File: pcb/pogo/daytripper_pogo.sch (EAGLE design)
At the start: 4 parts

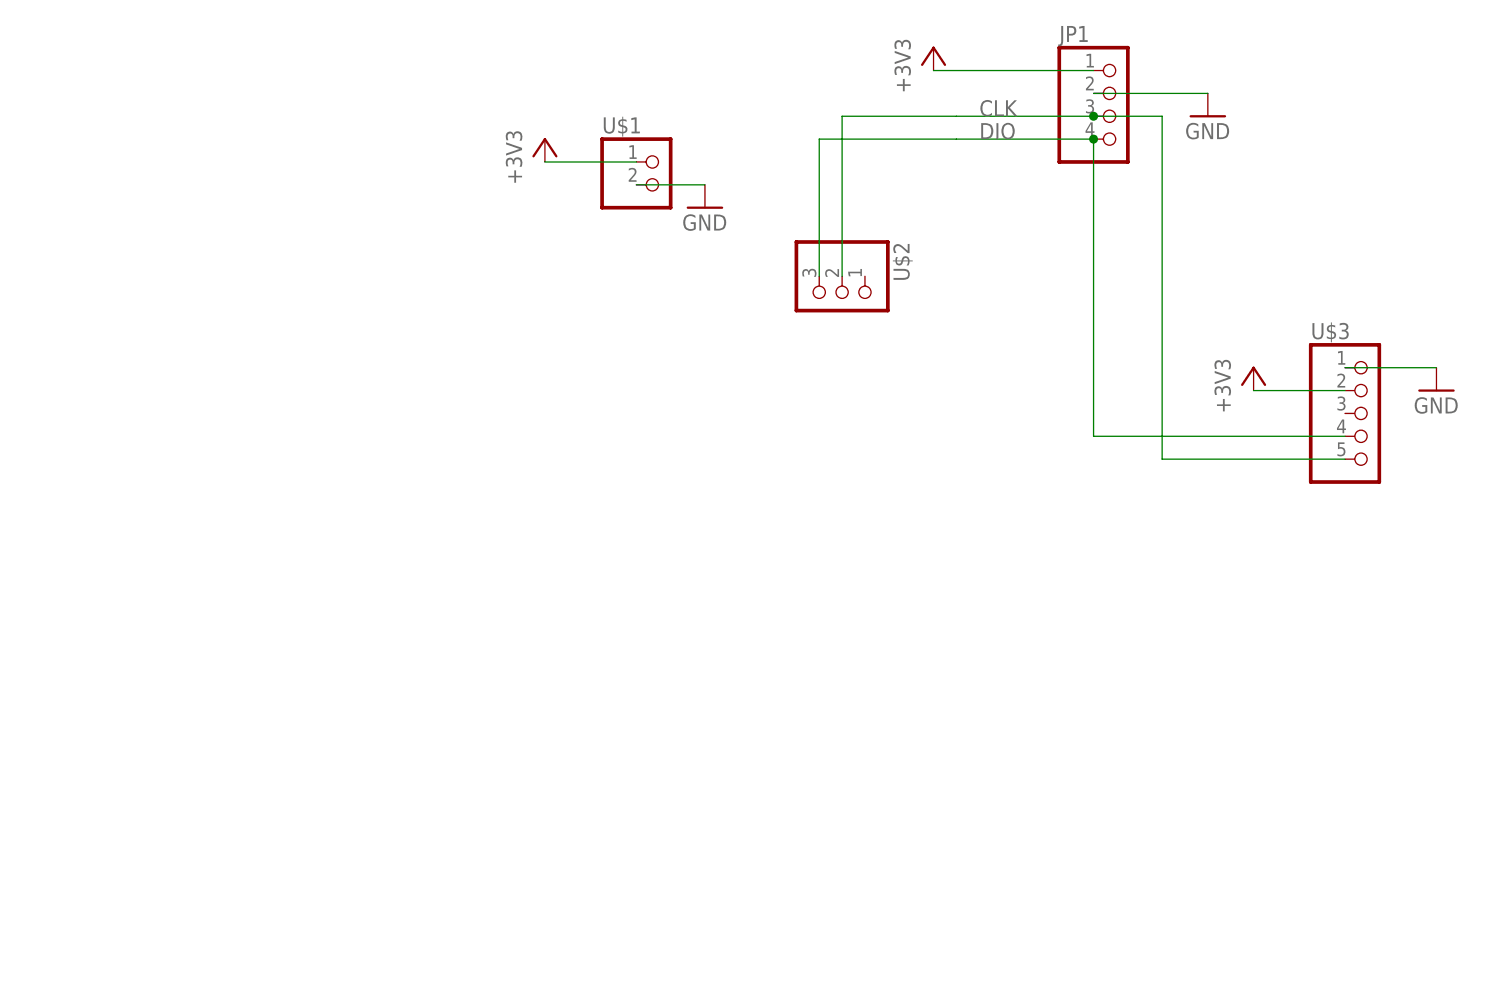
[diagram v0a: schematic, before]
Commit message: redesigned pogo board
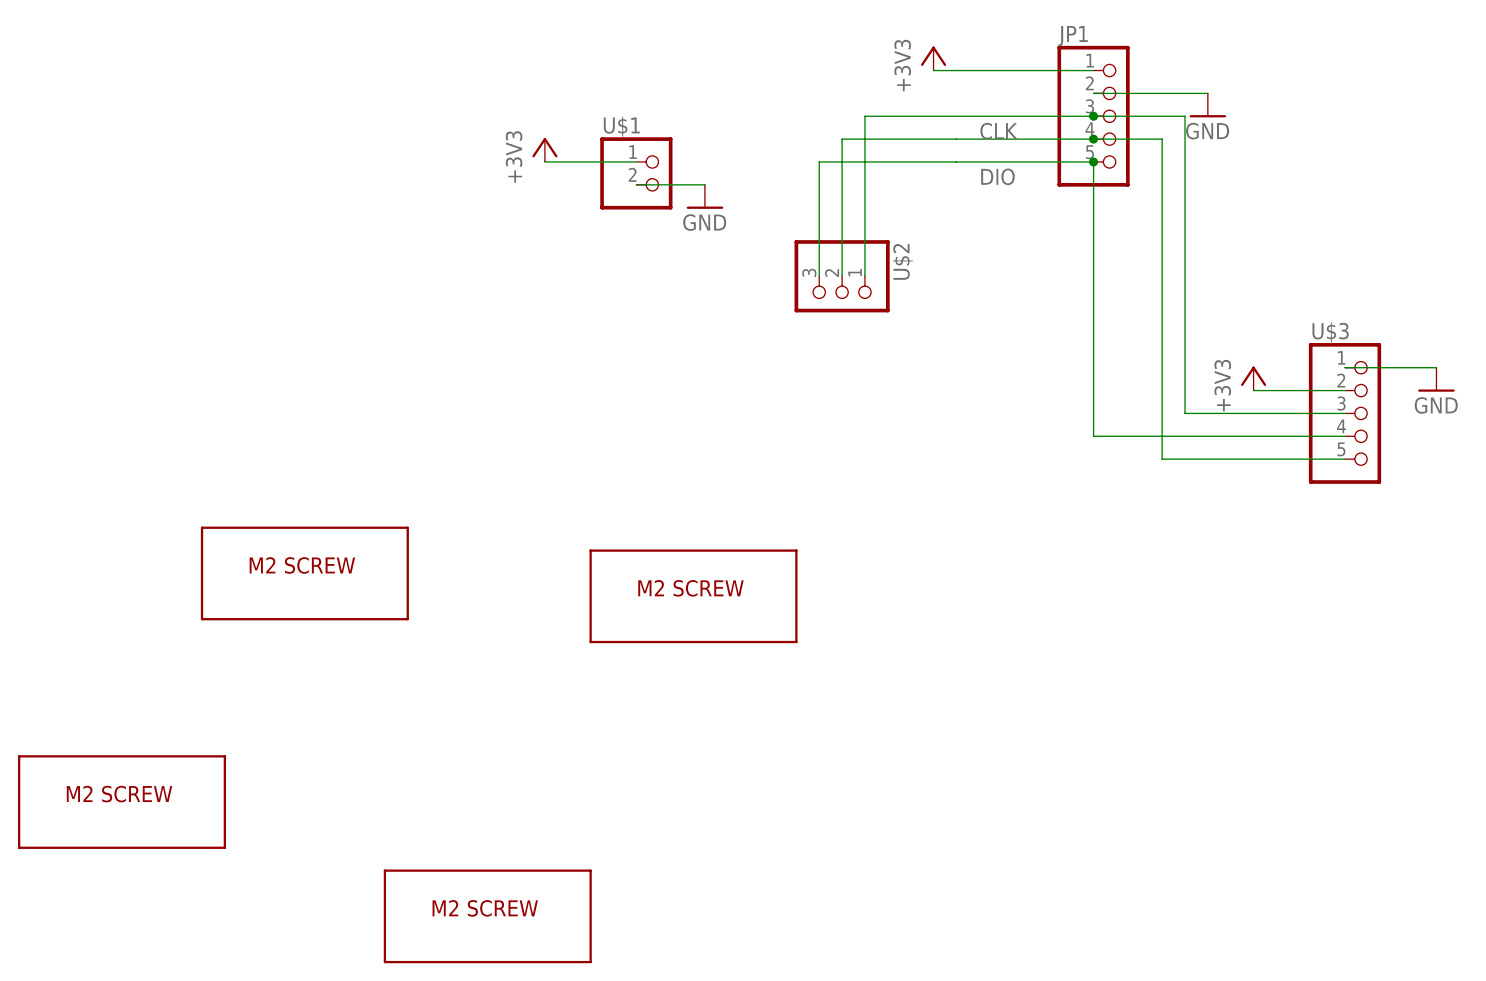
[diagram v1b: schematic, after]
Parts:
- added U$12, U$13, U$14, U$4: M2_SCREW_DEV, 3pos_slide_switch:M2_SCREW_DEV
- JP1: device pinhead:PINHD-1X4 -> pinhead:PINHD-1X5
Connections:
- new net N$1: JP1.3, U$2.1, U$3.3
- net CLK: now also JP1.4; no longer JP1.3
- net DIO: now also JP1.5; no longer JP1.4
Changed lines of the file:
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@@
 <part name="U$2" library="3pos_slide_switch" deviceset="POGO-1X3" device=""/>
 <part name="U$3" library="3pos_slide_switch" deviceset="POGO-1X5" device=""/>
-<part name="JP1" library="pinhead" library_urn="urn:adsk.eagle:library:325" deviceset="PINHD-1X4" device="" package3d_urn="urn:adsk.eagle:package:22407/2"/>
+<part name="JP1" library="pinhead" library_urn="urn:adsk.eagle:library:325" deviceset="PINHD-1X5" device="" package3d_urn="urn:adsk.eagle:package:22469/2"/>
 <part name="GND1" library="clock" deviceset="GND" device=""/>
 <part name="+3V1" library="supply1" library_urn="urn:adsk.eagle:library:371" deviceset="+3V3" device=""/>
 <part name="+3V2" library="supply1" library_urn="urn:adsk.eagle:library:371" deviceset="+3V3" device=""/>
 <part name="GND2" library="clock" deviceset="GND" device=""/>
+<part name="U$4" library="3pos_slide_switch" deviceset="M2_SCREW_DEV" device=""/>
+<part name="U$12" library="3pos_slide_switch" deviceset="M2_SCREW_DEV" device=""/>
+<part name="U$13" library="3pos_slide_switch" deviceset="M2_SCREW_DEV" device=""/>
+<part name="U$14" library="3pos_slide_switch" deviceset="M2_SCREW_DEV" device=""/>
 </parts>
 <sheets>
@@
 <instance part="+3V2" gate="G$1" x="-12.7" y="-7.62"/>
 <instance part="GND2" gate="1" x="5.08" y="-15.24"/>
+<instance part="U$4" gate="G$1" x="-40.64" y="-55.88"/>
+<instance part="U$12" gate="G$1" x="2.54" y="-58.42"/>
+<instance part="U$13" gate="G$1" x="-20.32" y="-93.98"/>
+<instance part="U$14" gate="G$1" x="-60.96" y="-81.28"/>
 </instances>
 <busses>
@@
 <net name="CLK" class="0">
 <segment>
-<pinref part="JP1" gate="A" pin="3"/>
-<wire x1="33.02" y1="-5.08" x2="48.26" y2="-5.08" width="0.1524" layer="91"/>
-<label x="35.56" y="-5.08" size="1.778" layer="95"/>
 <pinref part="U$2" gate="G$1" pin="2"/>
-<wire x1="33.02" y1="-5.08" x2="20.32" y2="-5.08" width="0.1524" layer="91"/>
-<wire x1="20.32" y1="-5.08" x2="20.32" y2="-22.86" width="0.1524" layer="91"/>
-<wire x1="48.26" y1="-5.08" x2="55.88" y2="-5.08" width="0.1524" layer="91"/>
-<wire x1="55.88" y1="-5.08" x2="55.88" y2="-43.18" width="0.1524" layer="91"/>
-<junction x="48.26" y="-5.08"/>
+<wire x1="33.02" y1="-7.62" x2="20.32" y2="-7.62" width="0.1524" layer="91"/>
+<wire x1="20.32" y1="-7.62" x2="20.32" y2="-22.86" width="0.1524" layer="91"/>
+<label x="35.56" y="-7.62" size="1.778" layer="95"/>
+<pinref part="JP1" gate="A" pin="4"/>
+<wire x1="33.02" y1="-7.62" x2="48.26" y2="-7.62" width="0.1524" layer="91"/>
+<wire x1="55.88" y1="-7.62" x2="55.88" y2="-43.18" width="0.1524" layer="91"/>
 <pinref part="U$3" gate="G$1" pin="5"/>
 <wire x1="55.88" y1="-43.18" x2="76.2" y2="-43.18" width="0.1524" layer="91"/>
+<wire x1="48.26" y1="-7.62" x2="55.88" y2="-7.62" width="0.1524" layer="91"/>
+<junction x="48.26" y="-7.62"/>
 </segment>
 </net>
 <net name="DIO" class="0">
 <segment>
-<pinref part="JP1" gate="A" pin="4"/>
-<wire x1="33.02" y1="-7.62" x2="48.26" y2="-7.62" width="0.1524" layer="91"/>
-<label x="35.56" y="-7.62" size="1.778" layer="95"/>
+<pinref part="U$3" gate="G$1" pin="4"/>
+<wire x1="48.26" y1="-40.64" x2="76.2" y2="-40.64" width="0.1524" layer="91"/>
 <pinref part="U$2" gate="G$1" pin="3"/>
-<wire x1="33.02" y1="-7.62" x2="17.78" y2="-7.62" width="0.1524" layer="91"/>
-<wire x1="17.78" y1="-7.62" x2="17.78" y2="-22.86" width="0.1524" layer="91"/>
-<pinref part="U$3" gate="G$1" pin="4"/>
-<wire x1="48.26" y1="-7.62" x2="48.26" y2="-40.64" width="0.1524" layer="91"/>
-<wire x1="48.26" y1="-40.64" x2="76.2" y2="-40.64" width="0.1524" layer="91"/>
-<junction x="48.26" y="-7.62"/>
+<wire x1="33.02" y1="-10.16" x2="17.78" y2="-10.16" width="0.1524" layer="91"/>
+<wire x1="17.78" y1="-10.16" x2="17.78" y2="-22.86" width="0.1524" layer="91"/>
+<label x="35.56" y="-12.7" size="1.778" layer="95"/>
+<pinref part="JP1" gate="A" pin="5"/>
+<wire x1="33.02" y1="-10.16" x2="48.26" y2="-10.16" width="0.1524" layer="91"/>
+<wire x1="48.26" y1="-40.64" x2="48.26" y2="-10.16" width="0.1524" layer="91"/>
+<junction x="48.26" y="-10.16"/>
 </segment>
 </net>
+<net name="N$1" class="0">
+<segment>
+<pinref part="U$2" gate="G$1" pin="1"/>
+<wire x1="22.86" y1="-22.86" x2="22.86" y2="-5.08" width="0.1524" layer="91"/>
+<pinref part="JP1" gate="A" pin="3"/>
+<wire x1="22.86" y1="-5.08" x2="48.26" y2="-5.08" width="0.1524" layer="91"/>
+<pinref part="U$3" gate="G$1" pin="3"/>
+<wire x1="76.2" y1="-38.1" x2="58.42" y2="-38.1" width="0.1524" layer="91"/>
+<wire x1="58.42" y1="-38.1" x2="58.42" y2="-5.08" width="0.1524" layer="91"/>
+<wire x1="58.42" y1="-5.08" x2="48.26" y2="-5.08" width="0.1524" layer="91"/>
+<junction x="48.26" y="-5.08"/>
+</segment>
+</net>
